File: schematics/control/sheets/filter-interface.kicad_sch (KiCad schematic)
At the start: 3 parts

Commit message: Updated VCA
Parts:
- removed RV_FILTER_RESO_1: 100k, Shmoergh_Custom_Footprints:NSL25_01x03_Vertical, symbol Device:R_Potentiometer
- added R46, R58, R59: 100k, symbol Device:R
- J_FILTER_INTERFACE_1: value Conn_01x08 -> Conn_01x05; footprint Shmoergh_Custom_Footprints:NSL25_01x08_Vertical -> (none); symbol Connector_Generic:Conn_01x08 -> Connector_Generic:Conn_01x05
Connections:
- net AUDIO_IN: now also J_FILTER_INTERFACE_1.1 (Pin_1); no longer J_FILTER_INTERFACE_1.8 (Pin_8)
- net AUDIO_OUT: now also J_FILTER_INTERFACE_1.5 (Pin_5); no longer J_FILTER_INTERFACE_1.1 (Pin_1)
- net GND: no longer J_FILTER_INTERFACE_1.6 (Pin_6), J_FILTER_INTERFACE_1.7 (Pin_7)
- net LFO_IN: now also R58.1; no longer J_FILTER_INTERFACE_1.5 (Pin_5)
- net at RV_FILTER_CUTOFF_1.2: now also R46.1; no longer J_FILTER_INTERFACE_1.2 (Pin_2)
- new net FILTER_CV: J_FILTER_INTERFACE_1.2 (Pin_2), R46.2, R58.2, R59.2
- new net FILTER_DIGITAL_MOD: R59.1
- no-connect marks 0 -> 2
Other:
- note added: "Filter CV inputs: - Cutoff frequency: pot - LFO - Modwheel (digital) - Envelope (digital) - Keyboard tracking (digital) - Velocity (digital) The last four is calculated and generated digitally by the microcontroller based on the incoming MIDI note/gate. It's coming from Channel B of the DAC. The rotary to select between the sources should be stereo so that it can send back signal to the MCU about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"
- note added: "TODO: - add rotary switch to select between filter CV sources"
- note removed: "TODO: - input for digital mod voltage (DCA ch. B) - rotary switch for cutoff mod source (envelope, LFO, digital) - filter mod amount potmeter Modwheel and keyboard tracking are both coming from the DCA's 2nd channel. The rotary should be stereo so that it can send a signal back to the MCU to select between kb tracking, modwheel or velocity as a mod source."
- moved on the sheet: RV_FILTER_CUTOFF_1

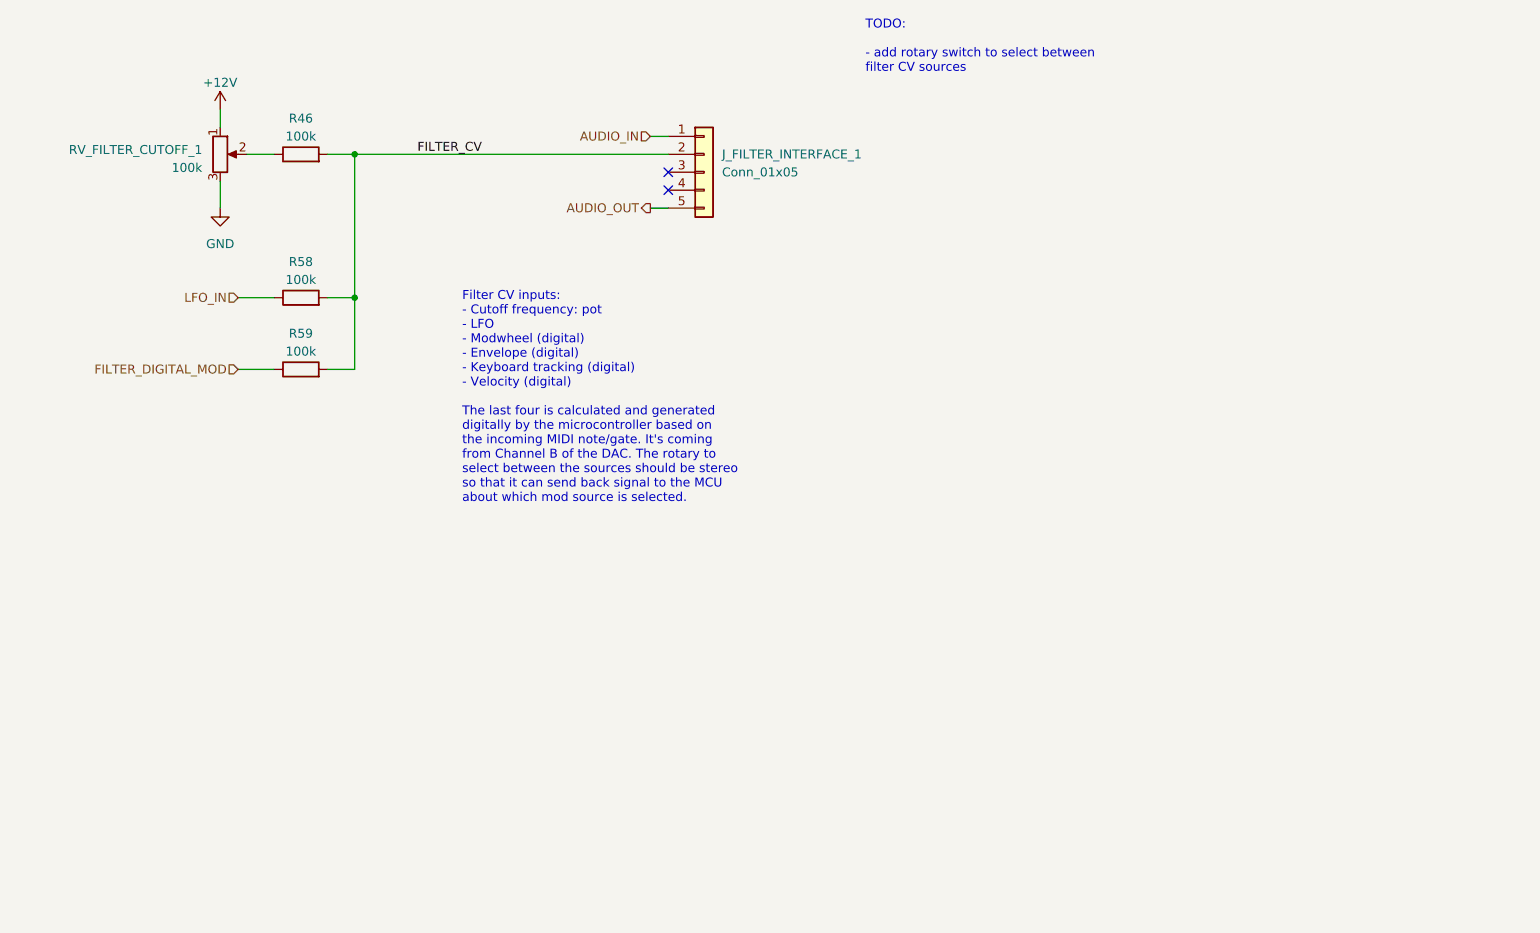
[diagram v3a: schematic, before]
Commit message: Added all UI components to schematics
- digital UI
- filter UI
- updated voice interface connection
- simplified schematics a lot
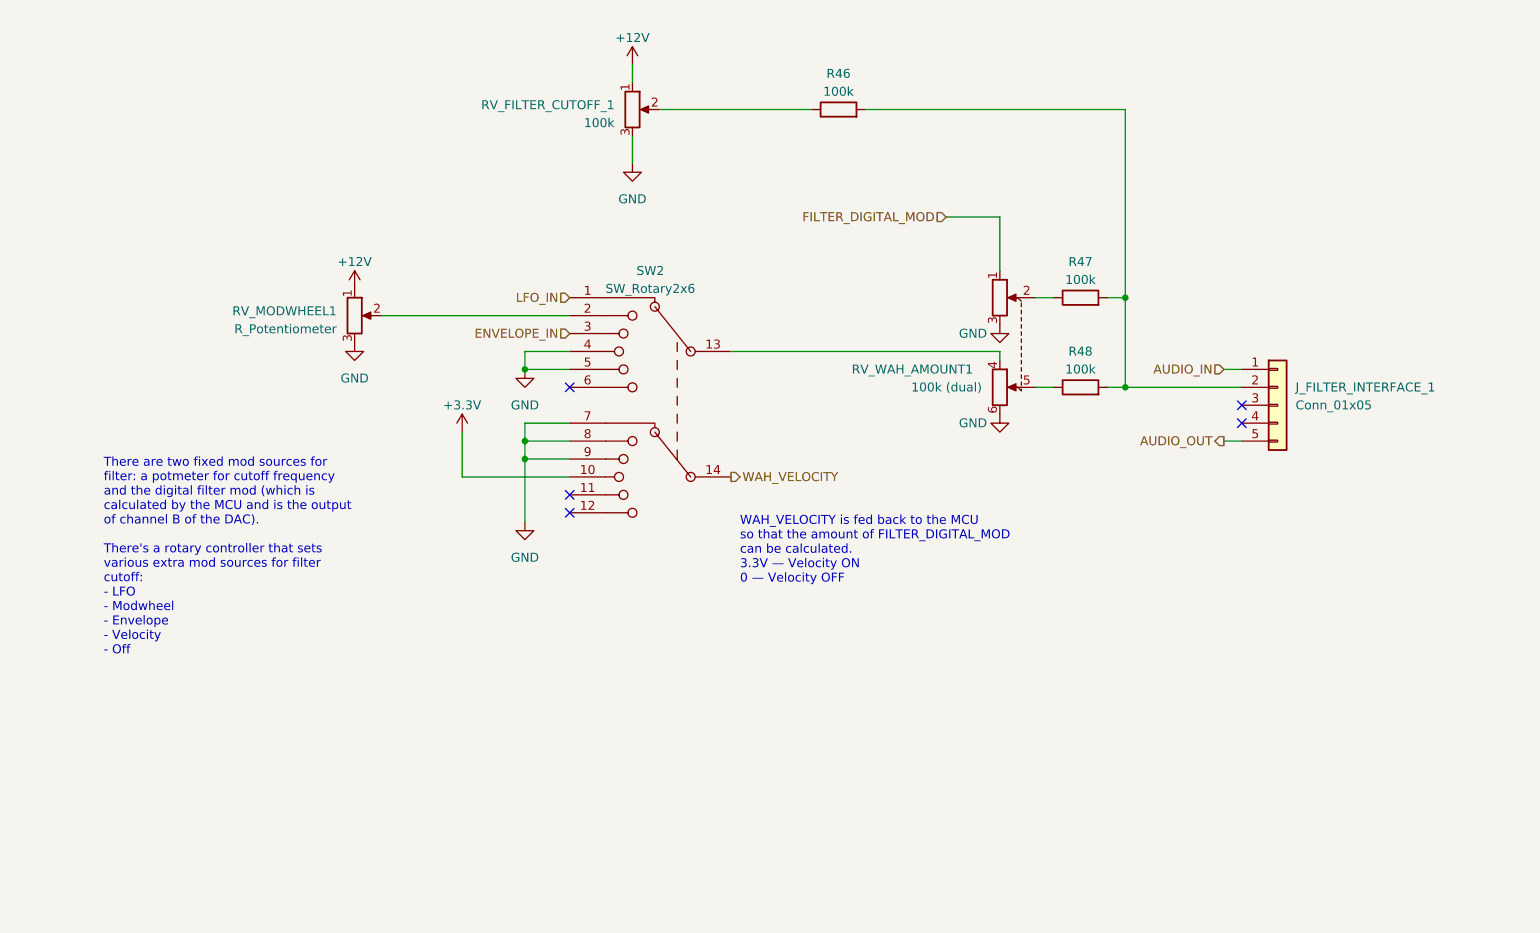
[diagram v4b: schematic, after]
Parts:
- removed R59: 100k, symbol Device:R
- added R47: 100k, symbol Device:R
- added RV_MODWHEEL1: R_Potentiometer, symbol Device:R_Potentiometer
- added RV_WAH_AMOUNT1: 100k (dual), symbol Device:R_Potentiometer_Dual
- added SW2: SW_Rotary2x6, symbol Switch:SW_Rotary2x6
- RV_FILTER_CUTOFF_1: footprint Shmoergh_Custom_Footprints:NSL25_01x03_Vertical -> (none)
- renumbered R58 to R48
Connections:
- net +12V: now also RV_MODWHEEL1.1
- net FILTER_DIGITAL_MOD: now also RV_WAH_AMOUNT1.1
- net GND: now also RV_MODWHEEL1.3, RV_WAH_AMOUNT1.3, RV_WAH_AMOUNT1.6, SW2.4, SW2.5, SW2.7, SW2.8, SW2.9
- net LFO_IN: now also SW2.1; no longer R48.1
- net FILTER_CV: no longer names the net of J_FILTER_INTERFACE_1.2 (Pin_2), R46.2, R48.2
- net FILTER_CV: now also R47.2
- new net: R47.1, RV_WAH_AMOUNT1.2
- new net: RV_WAH_AMOUNT1.4, SW2.13
- new net: RV_MODWHEEL1.2, SW2.2
- new net: R48.1, RV_WAH_AMOUNT1.5
- new net +3.3V: SW2.10
- new net ENVELOPE_IN: SW2.3
- new net WAH_VELOCITY: SW2.14
- no-connect marks 2 -> 5
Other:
- note added: "There are two fixed mod sources for filter: a potmeter for cutoff frequency and the digital filter mod (which is calculated by the MCU and is the output of channel B of the DAC). There's a rotary controller that sets various extra mod sources for filter cutoff: - LFO - Modwheel - Envelope - Velocity - Off"
- note added: "WAH_VELOCITY is fed back to the MCU so that the amount of FILTER_DIGITAL_MOD can be calculated. 3.3V — Velocity ON 0 — Velocity OFF"
- note removed: "Filter CV inputs: - Cutoff frequency: pot - LFO - Modwheel (digital) - Envelope (digital) - Keyboard tracking (digital) - Velocity (digital) The last four is calculated and generated digitally by the microcontroller based on the incoming MIDI note/gate. It's coming from Channel B of the DAC. The rotary to select between the sources should be stereo so that it can send back signal to the MCU about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"
- note removed: "TODO: - add rotary switch to select between filter CV sources"
- moved on the sheet: J_FILTER_INTERFACE_1, R46, R48, RV_FILTER_CUTOFF_1

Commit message: Schemo work
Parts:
- added J_FILTER_IO1, J_FILTER_IO2: Conn_01x06, Shmoergh_Custom_Footprints:NSL25_01x06_Vertical, symbol Connector_Generic:Conn_01x06
- #RV_FILTER_CUTOFF_1: renamed from RV_FILTER_CUTOFF_1; footprint (none) -> Shmoergh_Custom_Footprints:NSL25_01x03_Vertical
- #RV_MODWHEEL1: renamed from RV_MODWHEEL1; footprint (none) -> Shmoergh_Custom_Footprints:NSL25_01x03_Vertical
- #RV_WAH_AMOUNT1: renamed from RV_WAH_AMOUNT1; footprint (none) -> Shmoergh_Custom_Footprints:NSL25_01x06_Vertical
- J_FILTER_INTERFACE_1: footprint (none) -> Shmoergh_Custom_Footprints:NSL25_01x05_Vertical
- R46, R47, R48: footprint (none) -> Shmoergh_Custom_Footprints:R_Axial_DIN0207_L6.3mm_D2.5mm_P7.62mm_Horizontal
- renumbered SW2 to #SW2
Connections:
- net +12V: now also J_FILTER_IO1.1 (Pin_1)
- net +3.3V: now also J_FILTER_IO1.2 (Pin_2)
- net ENVELOPE_IN: now also J_FILTER_IO1.6 (Pin_6)
- net FILTER_DIGITAL_MOD: now also J_FILTER_IO2.2 (Pin_2)
- net GND: now also J_FILTER_IO2.5 (Pin_5), J_FILTER_IO2.6 (Pin_6)
- net LFO_IN: now also J_FILTER_IO1.5 (Pin_5)
- net WAH_VELOCITY: now also J_FILTER_IO2.1 (Pin_1)
- net CUTOFF_IN: now reaches #RV_FILTER_CUTOFF_1.2, R46.1
- net CUTOFF_IN: now also J_FILTER_IO1.3 (Pin_3)
- net FILTER_DIGI_MOD_IN: now reaches #RV_WAH_AMOUNT1.2, R47.1
- net FILTER_DIGI_MOD_IN: now also J_FILTER_IO2.3 (Pin_3)
- net WAH_ROTARY_IN: now reaches #RV_WAH_AMOUNT1.4, #SW2.13
- net MODWHEEL_IN: now reaches #RV_MODWHEEL1.2, #SW2.2
- net MODWHEEL_IN: now also J_FILTER_IO1.4 (Pin_4)
- net WAH_AMNT_IN: now reaches #RV_WAH_AMOUNT1.5, R48.1
- net WAH_AMNT_IN: now also J_FILTER_IO2.4 (Pin_4)
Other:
- note added: "All this has to be wired on the UI."
- moved on the sheet: J_FILTER_INTERFACE_1, R46, R47, R48
